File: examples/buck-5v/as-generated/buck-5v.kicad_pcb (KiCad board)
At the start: 2 copper layers, 126 x 56 mm, 11 parts, among them J1 12V IN, J2 5V OUT, U1 LM2596S-5

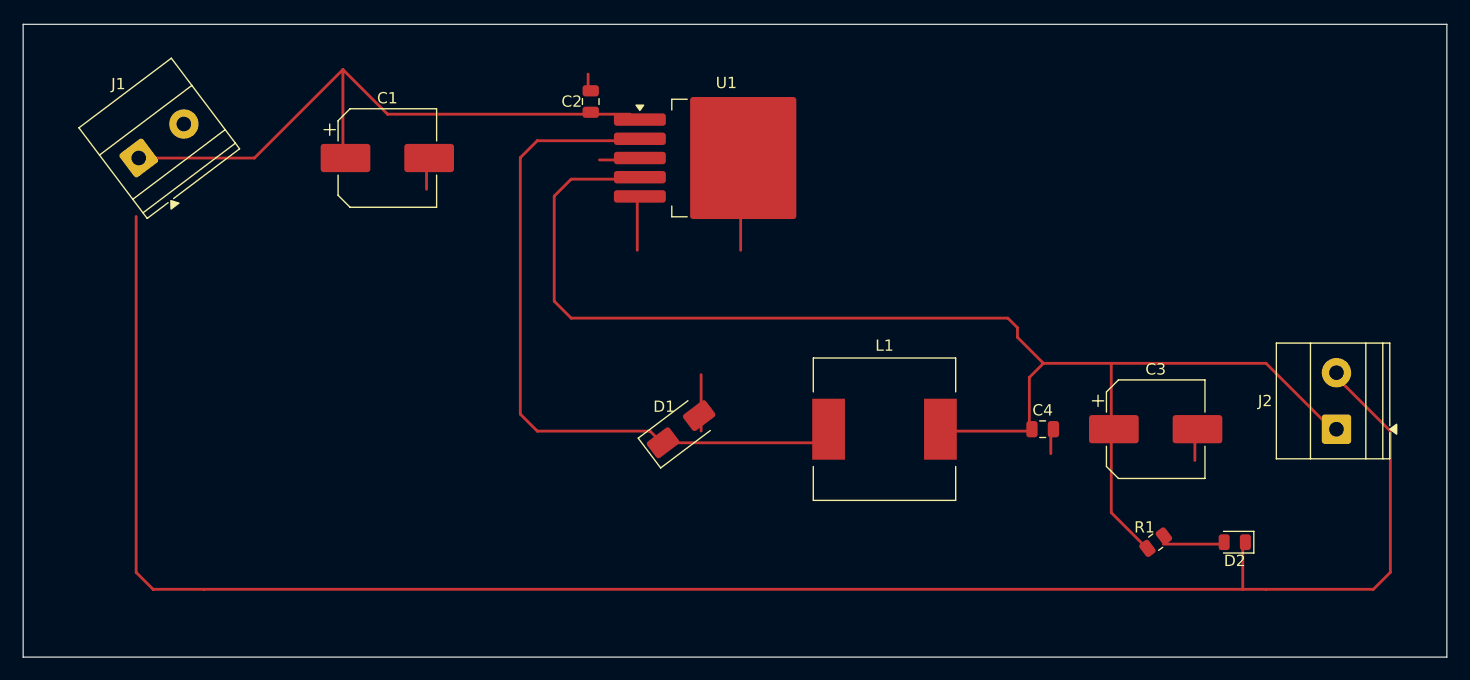
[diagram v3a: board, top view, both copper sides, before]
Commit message: Relieve the pads, fillet the joints, and give the board its screw holes
Three of the reviewer's manufacturing points, and they largely fall out
of the one before it - once KiCad fills the plane, the thermal relief it
was already asked for in the file actually appears.

**Thermal relief.** The zones said thermal all along; our own filler
ignored it and flooded every land solid. KiCad's does not, so every
through-hole ground pad now sits in a gap bridged by four spokes and an
iron can bring the joint up without heating a hundred square millimetres
of copper. `layout.solid_pad_connection` reports the setting when a
board turns it off: drilled pads only, because a surface pad reflows in
an oven that is heating the plane anyway and flooding it is often the
better thermal answer.

**Teardrops.** A track entering a land is a step change in width, and a
step change is where copper tears - the connector gets levered on and
off, the drill wanders, and the crack starts at the corner. `_teardrops`
replaces the first stretch of each run with a three-step taper into the
land, checked against its neighbours before it is kept, so a fillet
never eats the clearance a fine-pitch escape needs. It *replaces* rather
than overlays: laying the taper on top of the run drew the same copper
twice, and `route.acute_angle` reported all thirty of them, correctly.
`route.mixed_track_widths` learns what a fillet looks like so a properly
filleted board does not read as one nobody decided the width of.

**Mounting holes.** Four M3 holes near the corners, placed before the
router runs because they are obstacles, and slid along the edges or a
little inboard where a connector body has the corner - the motor board
and the op-amp take three, which is what those floorplans have room for.
Grounded on the motor driver, whose chassis is metal and part of the
shield, plain on the rest: bonding the enclosure to the reference is the
enclosure's decision, not the board's.

Two things that fell out of placing par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
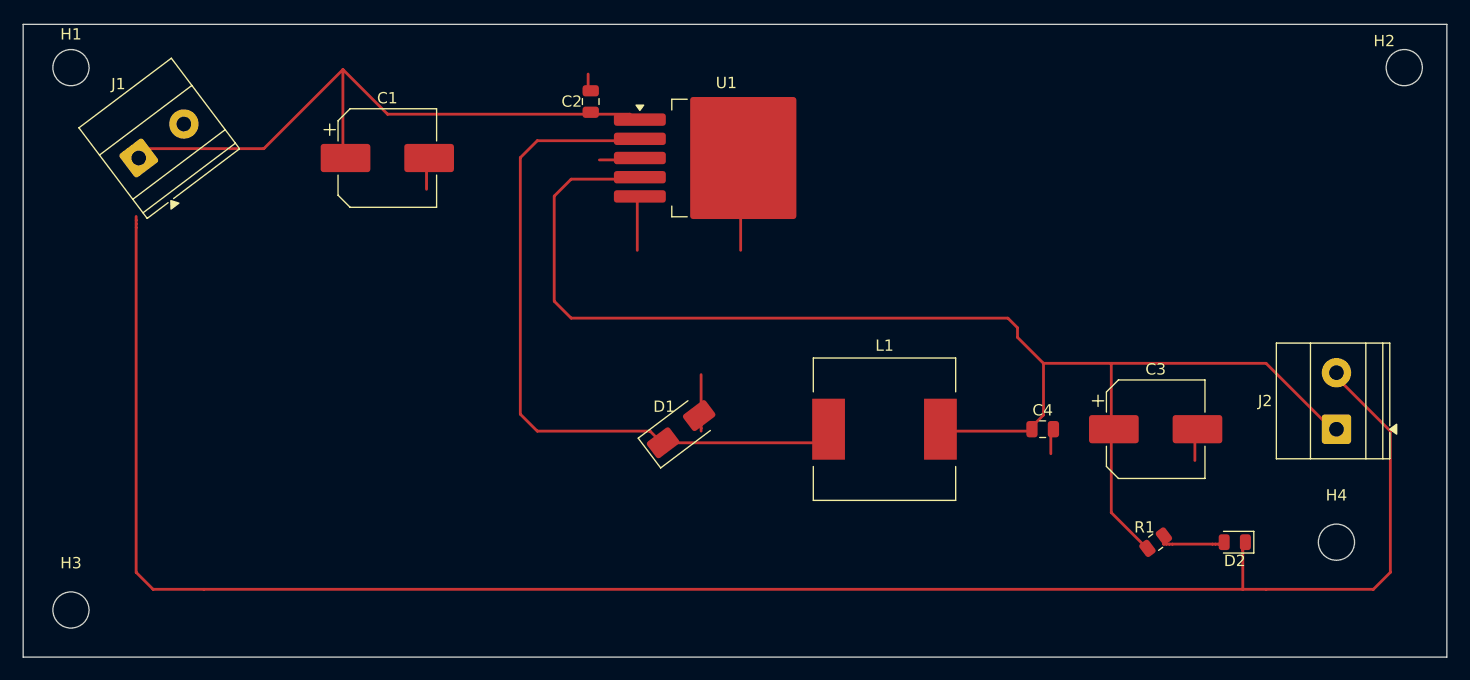
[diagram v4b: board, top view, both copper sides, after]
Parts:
- added H1: M33, MountingHole:MountingHole_3.2mm_M3, F.Cu at (104.2, 63.8)
- added H2: M33, MountingHole:MountingHole_3.2mm_M3, F.Cu at (222.2, 63.8)
- added H3: M33, MountingHole:MountingHole_3.2mm_M3, F.Cu at (104.2, 111.8)
- added H4: M33, MountingHole:MountingHole_3.2mm_M3, F.Cu at (216.2, 105.8)

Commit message: Give the assembly machine something to aim at
Fiducials: three copper dots in bare mask windows, near three different
corners so a pick-and-place gets rotation as well as offset. It aligns
to the board, not to the drawing - without them it has only the routed
outline, cut to a tolerance ten times looser than the placement a 0.5 mm
pitch part is asking for. `fab.no_fiducials` reports a fine-pitch board
that has none, as context rather than as a fault: plenty of boards are
built one at a time with tweezers.

They share the corner search with the mounting holes, which is where
this found a real bug: `_courtyard_box` read lines and rectangles only,
and a mounting hole draws its courtyard as one circle - so every hole
measured as taking up no room at all, and the first three fiducials
landed on top of three screw holes. Circles and arcs count now.

Co-Authored-By: Claude Fable 5 <noreply@anthropic.com>
Claude-Session: https://claude.ai/code/session_01DUj7Ltu92tWg159mCSacwY
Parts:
- added FID1: Fiducial, Fiducial:Fiducial_1mm_Mask2mm, F.Cu at (102.7, 69.3)
- added FID2: Fiducial, Fiducial:Fiducial_1mm_Mask2mm, F.Cu at (216.7, 62.3)
- added FID3: Fiducial, Fiducial:Fiducial_1mm_Mask2mm, F.Cu at (109.7, 113.3)
- H1, H2, H3, H4: value M33 -> M3

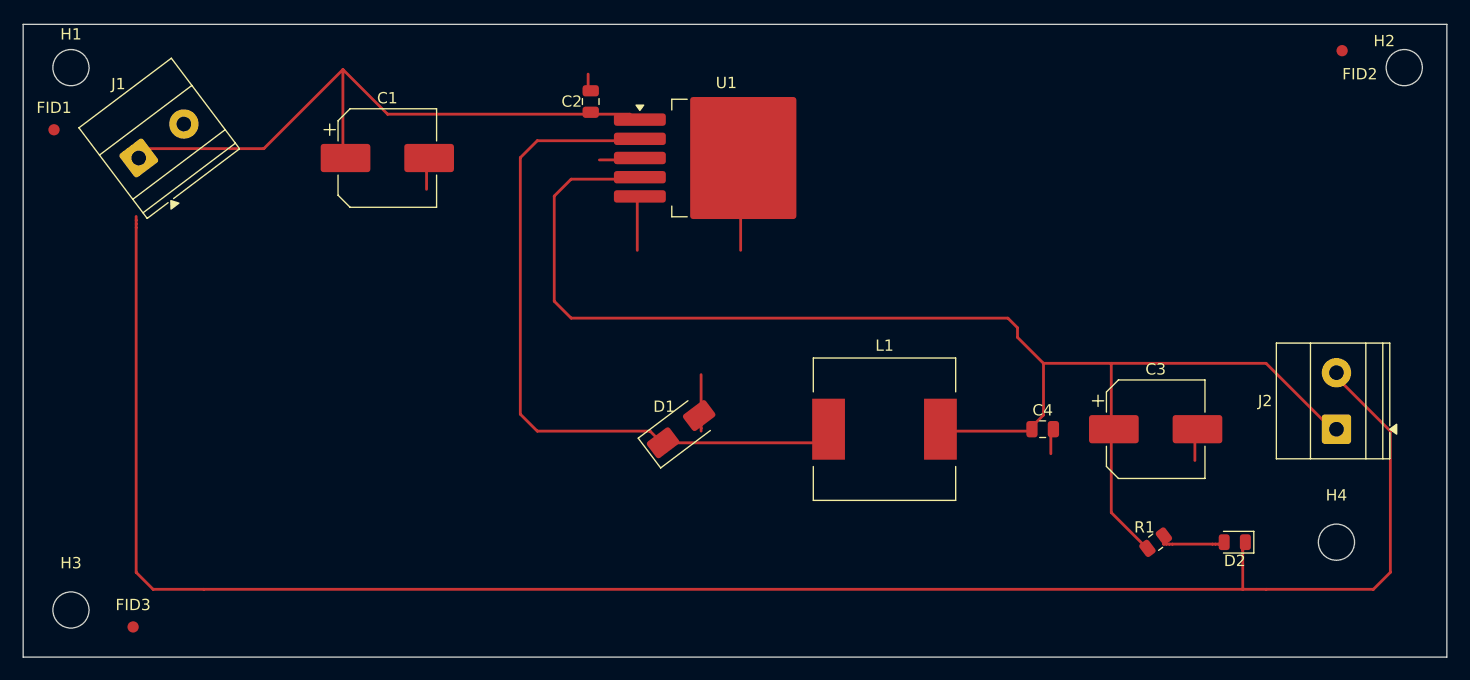
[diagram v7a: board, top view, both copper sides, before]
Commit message: Leave room for the screw, and print the ink where the board is
The screw holes were placed against the hole's own courtyard, which is the
drill plus a whisker - so on four of the five boards a hole sat inside a
connector's mating space, closest 0.42 mm. What goes through an M3 hole is a
pan head on a washer, seven millimetres of steel lying flat, and a connector
wants its shell, its wires and the fingers that fit them on top of that. The
spot search now keeps the fastener's own circle clear of every part body and
gives connectors CONNECTOR_ACCESS more, and three rules say so when a board
does not: mechanical.fastener_clearance, mechanical.connector_access and
mechanical.fastener_copper, all blocking for a generated design.

Silk was measured with a per-character advance of 0.78, and KiCad's stroke
font is proportional at 0.94 to 1.07. Everything downstream of that estimate
was placing ink where it did not fit: a legend across a capacitor's land, a
designator through the board's own name. `_text_extent` takes the top of the
measured range, adds the fab's clearance and is used by every silk placement.

Three placements also fell through to a position nobody chose. A designator
that found nothing kept its library offset, which for a part in a corner
points off the board; the board id took the first of eight fixed strips; a
legend took the least bad of six spots. All three are scored now, over
candidate sets wide enough to have an answer - and a pad-less footprint, which
is what a mounting hole is, is no longer skipped outright.

silk.off_board reports the case KiCad's own test cannot: ink that clears the
edge entirely is never printed, and DRC only measures ink that crosses it.

_unspiked redraws a corner tighter than a right angle as the elbow between its
neighbours - one diagonal, one straight, no step back to a heading the line
has already left. It is never longer than what it replaces.

All four fast boards: 0 errors, 0 warnings.

Co-Authored-By: Claude Fable 5 <no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
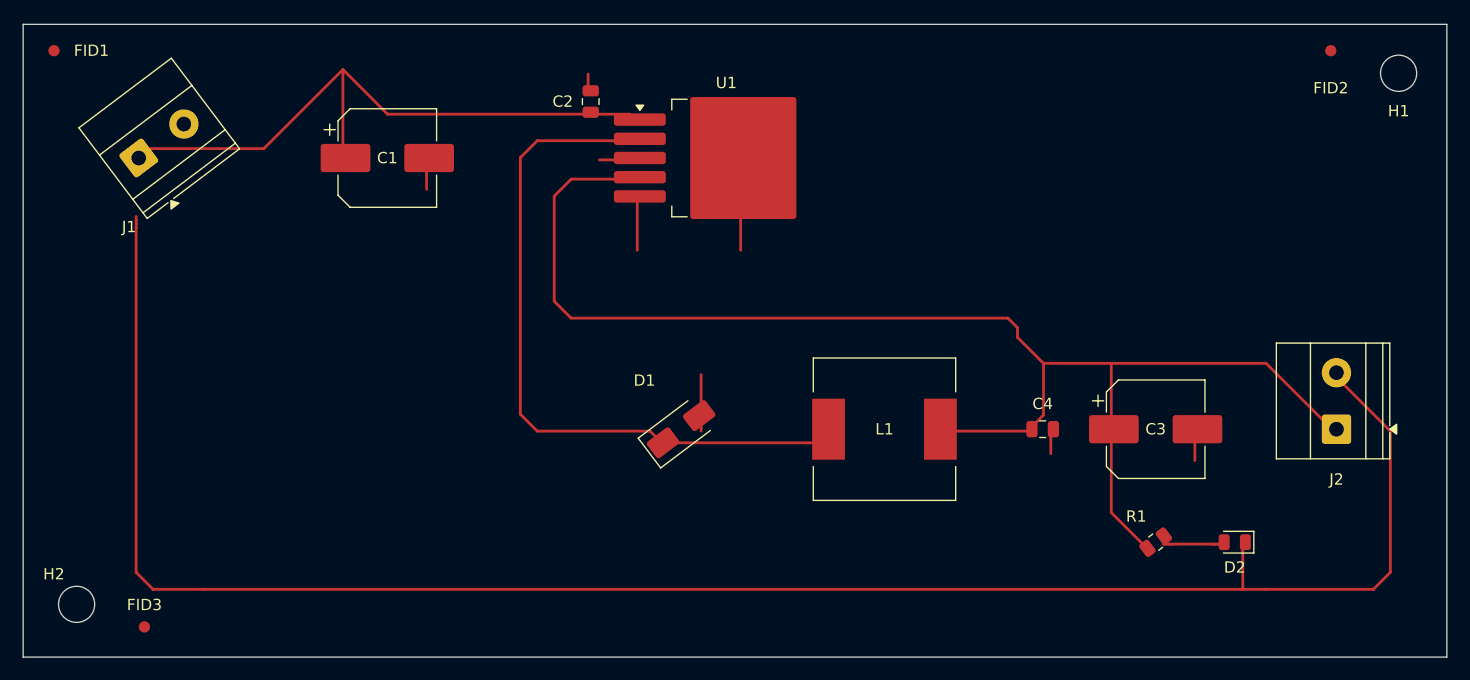
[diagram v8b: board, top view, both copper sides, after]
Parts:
- removed H3, H4: M3, MountingHole:MountingHole_3.2mm_M3
- moved H2 126.7 mm to (104.7, 111.3)
- moved H1 117.5 mm to (221.7, 64.3)
- moved FID1 7.00 mm to (102.7, 62.3)
- moved FID2 1.00 mm to (215.7, 62.3), turned to 0 degrees
- moved FID3 1.00 mm to (110.7, 113.3)
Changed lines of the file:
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@@
 		(tags "capacitor electrolytic")
 		(property "Reference" "C1"
-			(at 0 -5.3 0)
+			(at 0 0 0)
 			(layer "F.SilkS")
 			(effects
@@
 		)
 		(property "Datasheet" "https://industrial.panasonic.com/cdbs/www-data/pdf/RDF0000/ABA0000C1053.pdf"
-			(at 0 -5.3 0)
+			(at 0 0 0)
 			(layer "F.Fab")
 			(hide yes)
@@
 	(footprint "MountingHole:MountingHole_3.2mm_M3"
 		(layer "F.Cu")
-		(at 222.23 63.83 37)
+		(at 104.73 111.33 37)
 		(descr "Mounting Hole 3.2mm, M3, no annular, generated by kicad-footprint-generator mountinghole.py")
 		(tags "mountinghole M3")
 		(property "Reference" "H2"
-			(at 0 -2.95 0)
+			(at 0 -3.345 0)
 			(layer "F.SilkS")
 			(effects
@@
 		)
 		(property "Datasheet" "~"
-			(at 0 -2.95 0)
+			(at 0 -3.345 0)
 			(layer "F.Fab")
 			(hide yes)
@@
 		(tags "capacitor")
 		(property "Reference" "C4"
-			(at 0 -1.68 0)
+			(at 0 -2.245 0)
 			(layer "F.SilkS")
 			(effects
@@
 		)
 		(property "Datasheet" "https://product.samsungsem.com/mlcc/CL21B104KBCNNNC.do"
-			(at 0 -1.68 0)
+			(at 0 -2.245 0)
 			(layer "F.Fab")
 			(hide yes)
@@
 		(tags "THT Terminal Block Phoenix MKDS-1,5-2 pitch 5mm size 10x9.8mm drill 1.3mm pad 2.6mm")
 		(property "Reference" "J2"
-			(at 2.5 -6.32 0)
+			(at -4.445 0 0)
 			(layer "F.SilkS")
 			(effects
@@
 		)
 		(property "Datasheet" "https://www.phoenixcontact.com/product/1729128"
-			(at 2.5 -6.32 0)
+			(at -4.445 0 0)
 			(layer "F.Fab")
 			(hide yes)
@@
 		)
 	)
-	(footprint "MountingHole:MountingHole_3.2mm_M3"
-		(layer "F.Cu")
-		(at 216.23 105.83)
-		(descr "Mounting Hole 3.2mm, M3, no annular, generated by kicad-footprint-generator mountinghole.py")
-		(tags "mountinghole M3")
-		(property "Reference" "H4"
-			(at 0 -4.15 0)
-			(layer "F.SilkS")
-			(effects
-				(font
-					(size 1 1)
-					(thickness 0.15)
-				)
-			)
-		)
-		(property "Value" "M3"
-			(at 0 4.15 0)
-			(layer "F.Fab")
-			(effects
-				(font
-					(size 1 1)
-					(thickness 0.15)
-				)
-			)
-		)
-		(property "Datasheet" "~"
-			(at 0 -4.15 0)
-			(layer "F.Fab")
-			(hide yes)
-			(effects
-				(font
-					(size 1 1)
-					(thickness 0.15)
-				)
-			)
-		)
-		(property "Description" ""
-			(at 0 0 0)
-			(layer "F.Fab")
-			(hide yes)
-			(effects
-				(font
-					(size 1.27 1.27)
-					(thickness 0.15)
-				)
-			)
-		)
-		(attr exclude_from_pos_files exclude_from_bom)
-		(fp_circle
-			(center 0 0)
-			(end 3.2 0)
-			(stroke
-				(width 0.15)
-				(type solid)
-			)
-			(fill no)
-			(layer "Cmts.User")
-		)
-		(fp_circle
-			(center 0 0)
-			(end 3.45 0)
-			(stroke
-				(width 0.05)
-				(type solid)
-			)
-			(fill no)
-			(layer "F.CrtYd")
-		)
-		(fp_text user "${REFERENCE}"
-			(at 0 0 0)
-			(layer "F.Fab")
-			(effects
-				(font
-					(size 1 1)
-					(thickness 0.15)
-				)
-			)
-		)
-		(pad "" np_thru_hole circle
-			(at 0 0)
-			(size 3.2 3.2)
-			(drill 3.2)
-			(layers "*.Cu" "*.Mask")
-		)
-		(embedded_fonts no)
-	)
 	(footprint "LED_SMD:LED_0805_2012Metric"
 		(layer "F.Cu")
@@
 		(tags "LED")
 		(property "Reference" "D2"
-			(at 0 -1.65 0)
+			(at 0 -2.232 0)
 			(layer "F.SilkS")
 			(effects
@@
 		)
 		(property "Datasheet" "https://optoelectronics.liteon.com/upload/download/DS-22-98-0002/LTST-C170KGKT.pdf"
-			(at 0 -1.65 0)
+			(at 0 -2.232 0)
 			(layer "F.Fab")
 			(hide yes)
@@
 		(tags "capacitor electrolytic")
 		(property "Reference" "C3"
-			(at 0 -5.3 0)
+			(at 0 0 0)
 			(layer "F.SilkS")
 			(effects
@@
 		)
 		(property "Datasheet" "https://industrial.panasonic.com/cdbs/www-data/pdf/RDF0000/ABA0000C1053.pdf"
-			(at 0 -5.3 0)
+			(at 0 0 0)
 			(layer "F.Fab")
 			(hide yes)
@@
 		(tags "Diode SMA (DO-214AC)")
 		(property "Reference" "D1"
-			(at 0 -2.5 0)
+			(at 0 -5.395 0)
 			(layer "F.SilkS")
 			(effects
@@
 	(footprint "Fiducial:Fiducial_1mm_Mask2mm"
 		(layer "F.Cu")
-		(at 216.73 62.33 37)
+		(at 215.73 62.33)
 		(descr "Fiducial, circular marking, 1mm bare copper, 2mm soldermask opening (Level A)")
 		(tags "fiducial")
 		(property "Reference" "FID2"
-			(at 0 2.6 0)
+			(at 0 3.315 0)
 			(layer "F.SilkS")
 			(effects
@@
 		)
 		(property "Datasheet" "~"
-			(at 0 2.6 0)
+			(at 0 3.315 0)
 			(layer "F.Fab")
 			(hide yes)
@@
 		)
 		(property "Description" ""
-			(at 0 0 37)
+			(at 0 0 0)
 			(layer "F.Fab")
 			(hide yes)
@@
 		)
 		(pad "" smd circle
-			(at 0 0 37)
+			(at 0 0)
 			(size 1 1)
 			(layers "F.Cu" "F.Mask")
@@
 		(tags "Choke SMD")
 		(property "Reference" "L1"
-			(at 0 -7.4 0)
+			(at 0 0 0)
 			(layer "F.SilkS")
 			(effects
@@
 		(tags "THT Terminal Block Phoenix MKDS-1,5-2 pitch 5mm size 10x9.8mm drill 1.3mm pad 2.6mm")
 		(property "Reference" "J1"
-			(at 2.5 -6.32 0)
+			(at -4.356 4.356 0)
 			(layer "F.SilkS")
 			(effects
@@
 		)
 		(property "Datasheet" "https://www.phoenixcontact.com/product/1729128"
-			(at 2.5 -6.32 0)
+			(at -4.356 4.356 0)
 			(layer "F.Fab")
 			(hide yes)
@@
 		)
 	)
-	(footprint "MountingHole:MountingHole_3.2mm_M3"
-		(layer "F.Cu")
-		(at 104.23 111.83)
-		(descr "Mounting Hole 3.2mm, M3, no annular, generated by kicad-footprint-generator mountinghole.py")
-		(tags "mountinghole M3")
-		(property "Reference" "H3"
-			(at 0 -4.15 0)
-			(layer "F.SilkS")
-			(effects
-				(font
-					(size 1 1)
-					(thickness 0.15)
-				)
-			)
-		)
-		(property "Value" "M3"
-			(at 0 4.15 0)
-			(layer "F.Fab")
-			(effects
-				(font
-					(size 1 1)
-					(thickness 0.15)
-				)
-			)
-		)
-		(property "Datasheet" "~"
-			(at 0 -4.15 0)
-			(layer "F.Fab")
-			(hide yes)
-			(effects
-				(font
-					(size 1 1)
-					(thickness 0.15)
-				)
-			)
-		)
-		(property "Description" ""
-			(at 0 0 0)
-			(layer "F.Fab")
-			(hide yes)
-			(effects
-				(font
-					(size 1.27 1.27)
-					(thickness 0.15)
-				)
-			)
-		)
-		(attr exclude_from_pos_files exclude_from_bom)
-		(fp_circle
-			(center 0 0)
-			(end 3.2 0)
-			(stroke
-				(width 0.15)
-				(type solid)
-			)
-			(fill no)
-			(layer "Cmts.User")
-		)
-		(fp_circle
-			(center 0 0)
-			(end 3.45 0)
-			(stroke
-				(width 0.05)
-				(type solid)
-			)
-			(fill no)
-			(layer "F.CrtYd")
-		)
-		(fp_text user "${REFERENCE}"
-			(at 0 0 0)
-			(layer "F.Fab")
-			(effects
-				(font
-					(size 1 1)
-					(thickness 0.15)
-				)
-			)
-		)
-		(pad "" np_thru_hole circle
-			(at 0 0)
-			(size 3.2 3.2)
-			(drill 3.2)
-			(layers "*.Cu" "*.Mask")
-		)
-		(embedded_fonts no)
-	)
 	(footprint "Capacitor_SMD:C_0805_2012Metric"
 		(layer "F.Cu")
@@
 		(tags "capacitor")
 		(property "Reference" "C2"
-			(at 0 -1.68 0)
+			(at 0 -2.47 0)
 			(layer "F.SilkS")
 			(effects
@@
 		)
 		(property "Datasheet" "https://product.samsungsem.com/mlcc/CL21B104KBCNNNC.do"
-			(at 0 -1.68 0)
+			(at 0 -2.47 0)
 			(layer "F.Fab")
 			(hide yes)
@@
 		(tags "resistor")
 		(property "Reference" "R1"
-			(at 0 -1.65 0)
+			(at 0 -2.858 0)
 			(layer "F.SilkS")
 			(effects
@@
 		)
 		(property "Datasheet" "https://www.yageo.com/upload/media/product/productsearch/datasheet/rchip/PYu-RC_Group_51_RoHS_L_12.pdf"
-			(at 0 -1.65 0)
+			(at 0 -2.858 0)
 			(layer "F.Fab")
 			(hide yes)
@@
 	(footprint "Fiducial:Fiducial_1mm_Mask2mm"
 		(layer "F.Cu")
-		(at 109.73 113.33)
+		(at 110.73 113.33)
 		(descr "Fiducial, circular marking, 1mm bare copper, 2mm soldermask opening (Level A)")
 		(tags "fiducial")
@@
 	(footprint "MountingHole:MountingHole_3.2mm_M3"
 		(layer "F.Cu")
-		(at 104.23 63.83)
+		(at 221.73 64.33)
 		(descr "Mounting Hole 3.2mm, M3, no annular, generated by kicad-footprint-generator mountinghole.py")
 		(tags "mountinghole M3")
 		(property "Reference" "H1"
-			(at 0 -2.95 0)
+			(at 0 3.345 0)
 			(layer "F.SilkS")
 			(effects
@@
 		)
 		(property "Datasheet" "~"
-			(at 0 -2.95 0)
+			(at 0 3.345 0)
 			(layer "F.Fab")
 			(hide yes)
@@
 	(footprint "Fiducial:Fiducial_1mm_Mask2mm"
 		(layer "F.Cu")
-		(at 102.73 69.33)
+		(at 102.73 62.33)
 		(descr "Fiducial, circular marking, 1mm bare copper, 2mm soldermask opening (Level A)")
 		(tags "fiducial")
 		(property "Reference" "FID1"
-			(at 0 -1.95 0)
+			(at 3.315 0 0)
 			(layer "F.SilkS")
 			(effects
@@
 		)
 		(property "Datasheet" "~"
-			(at 0 -1.95 0)
+			(at 3.315 0 0)
 			(layer "F.Fab")
 			(hide yes)
